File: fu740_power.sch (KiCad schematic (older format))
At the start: 46 parts, among them J21 Conn_01x02_Male, J22 Conn_02x10_Odd_Even, M5 MountingHole_Pad, M6 MountingHole_Pad, M7 MountingHole_Pad, M8 MountingHole_Pad, U1 FU740-C000

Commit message: Project update
Schematic capture update.
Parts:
- removed C1, C2, C3, C4, C? (x5): 4.7uF, symbol Device:C_Small
- removed C? (x24): 0.1uF, symbol Device:C_Small
- added C? (x27): 0.1uF, symbol Device:C_Small
- added C? (x9): 4.7uF, symbol Device:C_Small
- added R?: 0.20ohm, symbol Device:R
- C5, C?: Voltage rating (none) -> 10V
- R?: value 0 -> 0.001ohm
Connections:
- net labels added: VDDSENSE, VDD_PLL, VDD_PLL_1V8, VSSSENSE
- wire segments 641 -> 672
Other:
- note added: "Current sensing resistor"

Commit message: Project update
Schematic capture update.
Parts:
- added C? (x2): 1uF, symbol Device:C_Small
- added J? (x2): Conn_01x03_Male, symbol Connector:Conn_01x03_Male
- added Q? (x2): IRLML6402TRPBF, symbol Device:Q_PMOS_GSD
- added Q? (x6): Q_DUAL_NMOS_G1S2G2D2S1D1, symbol Device:Q_DUAL_NMOS_G1S2G2D2S1D1
- added R? (x4): 100k, symbol Device:R
- added R? (x2): DNP, symbol Device:R
- added R? (x2): 4.7K, symbol Device:R
- added TP? (x2): TestPoint, symbol Connector:TestPoint
- C?: Voltage rating (none) -> 25V
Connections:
- net labels added: I2C0_SCL, I2C0_SCL_3V3, I2C0_SDA, I2C0_SDA_3V3, PWM1_2, PWM1_3, VDD_1V8, VDD_3V3
- wire segments 672 -> 732
- no-connect marks 0 -> 8
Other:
- note added: "I2C_0 level shift \n"
- note added: "Power measurement header"
- note added: "VDD_CPU Current sensing circuit"
- note added: "VDD_CPU bypass capacitors"
- note added: "VDD_PLL Current sensing circuit"
- note added: "VDD_PLL bypass capacitors"
- note removed: "Power measurement header\nAnalize if this can be not populated or removed."
- moved on the sheet: C?, R?, TP?

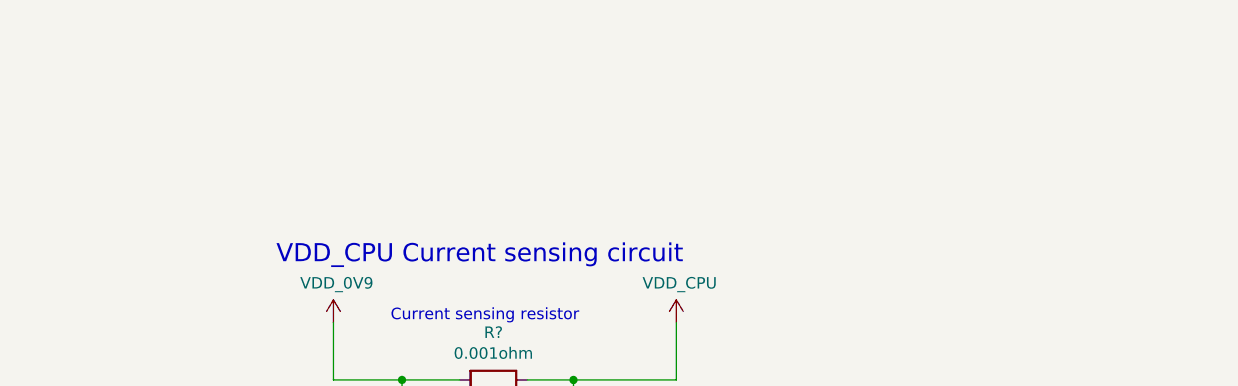
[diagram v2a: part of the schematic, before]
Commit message: Schematic capture update.
Schematic capture update.
DDR4 RAM page updated.
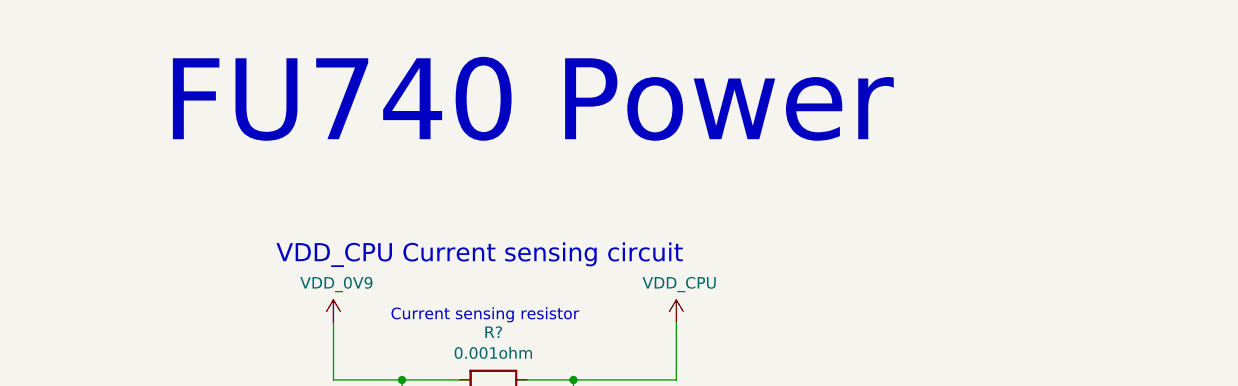
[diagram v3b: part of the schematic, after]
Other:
- note added: "FU740 Power"
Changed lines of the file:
@@
 Text Notes 10400 1450 0    79   ~ 0
 VDD_CPU Current sensing circuit
+Text Notes 9900 950  0    354  ~ 0
+FU740 Power
 $EndSCHEMATC
